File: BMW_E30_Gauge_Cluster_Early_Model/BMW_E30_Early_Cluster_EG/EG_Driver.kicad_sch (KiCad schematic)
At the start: 24 parts, among them Q2 BC337, U1 4049, U2 4584, U3 SAJ300R, U4 LM2903, U6 PIC1655A, Y1 160 kHz

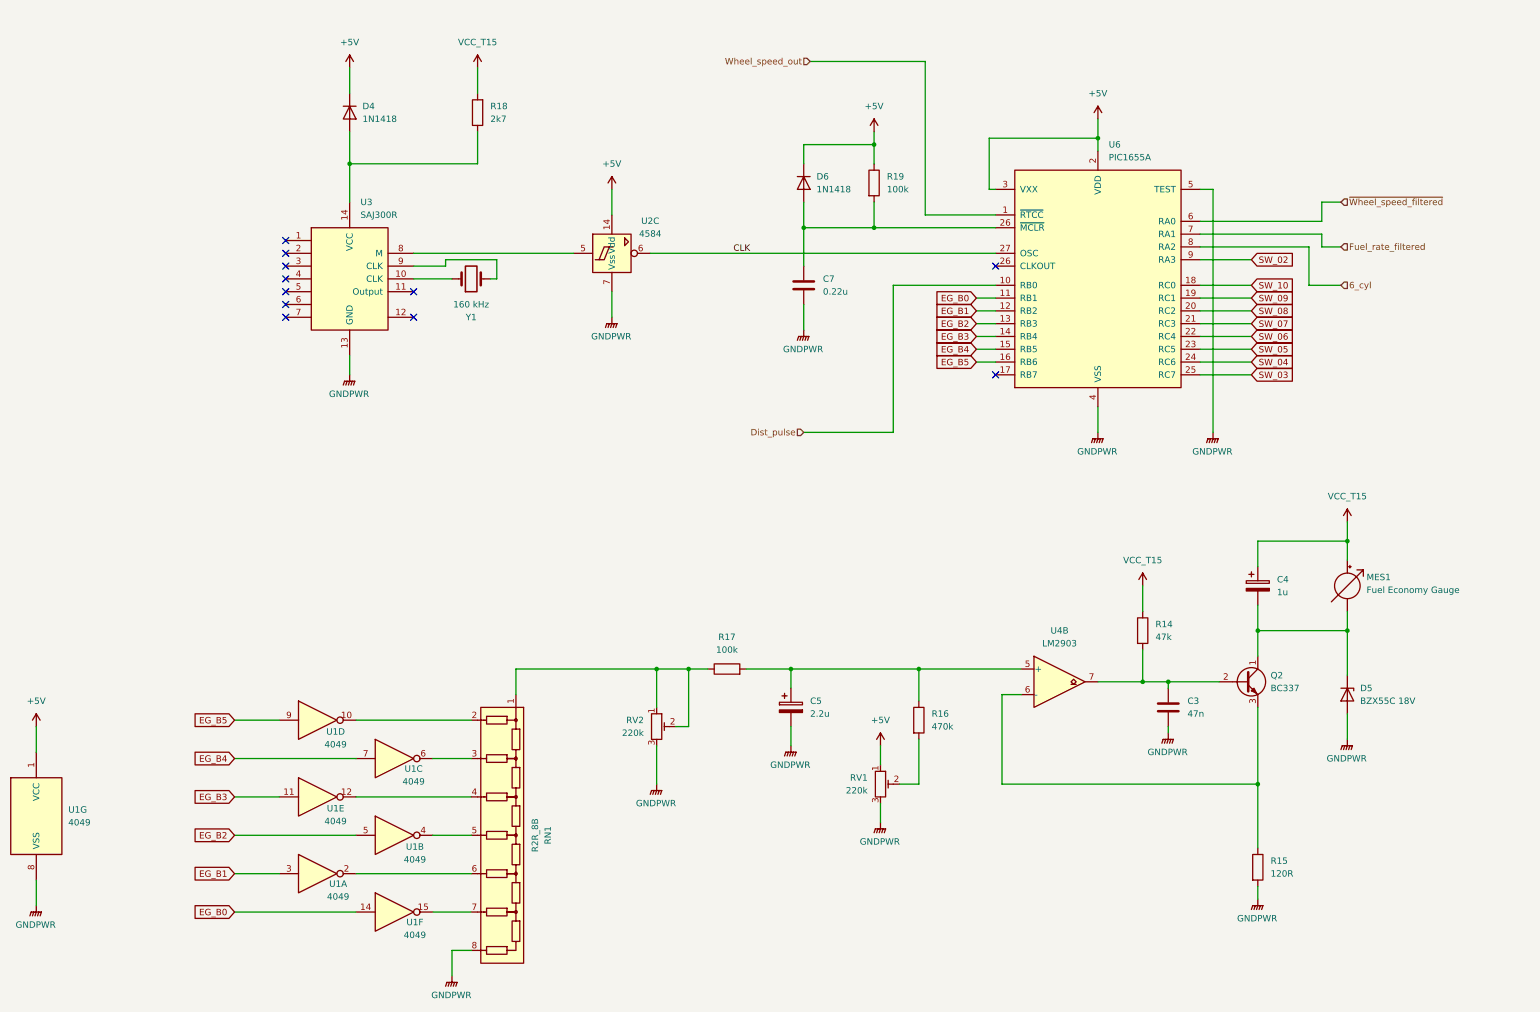
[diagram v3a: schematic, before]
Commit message: Layout Updates
Added footprints for coding plug, econometer gauge, and D5.

Also fixed pin number 28 on U6.
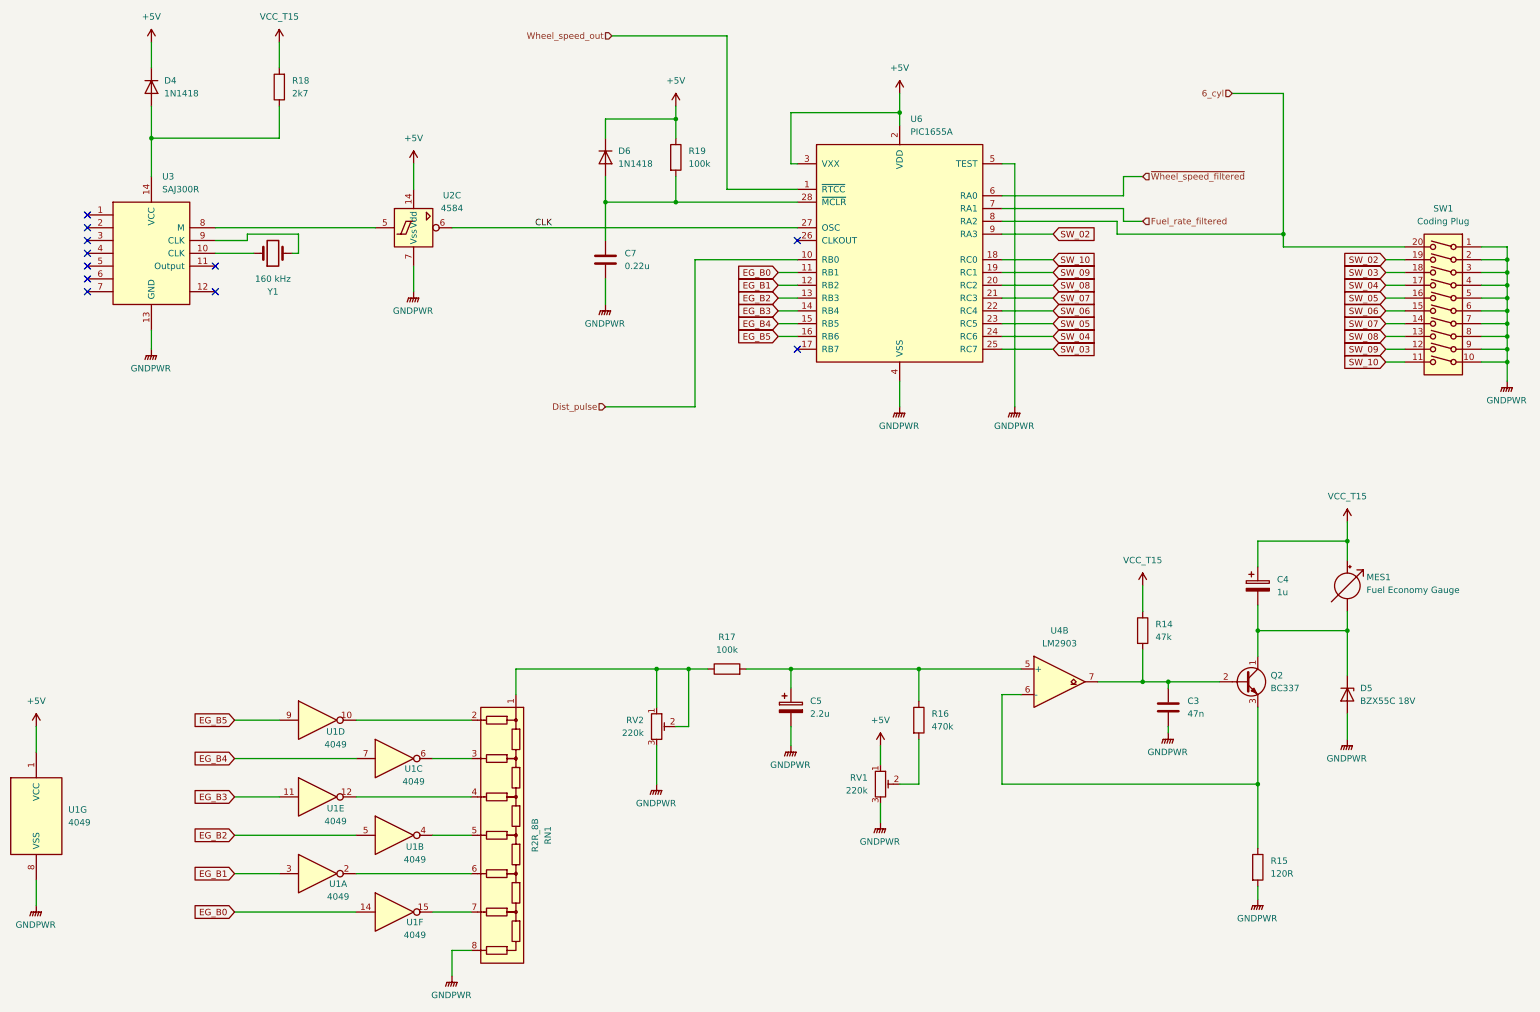
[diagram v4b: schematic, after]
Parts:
- added SW1: Coding Plug, BMW_Cluster_Connectors:Coding_Plug, symbol Switch:SW_DIP_x10
- D5: footprint (none) -> Diode_THT:D_DO-34_SOD68_P10.16mm_Horizontal
- MES1: footprint (none) -> BMW_Cluster_Connectors:Connector_EG
- U6: footprint Package_DIP:DIP-28_W15.24mm_Socket_LongPads -> Package_DIP:DIP-28_W15.24mm
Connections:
- net 6_cyl: now also SW1.20
- net GNDPWR: now also SW1.1, SW1.10, SW1.2, SW1.3, SW1.4, SW1.5, SW1.6, SW1.7, SW1.8, SW1.9
- net SW_02: now also SW1.19
- net SW_03: now also SW1.18
- net SW_04: now also SW1.17
- net SW_05: now also SW1.16
- net SW_06: now also SW1.15
- net SW_07: now also SW1.14
- net SW_08: now also SW1.13
- net SW_09: now also SW1.12
- net SW_10: now also SW1.11
- net at C7.1, D6.2 (A), R19.2: now also U6.28 (~{MCLR}); no longer U6.26 (CLKOUT)
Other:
- moved on the sheet: C7, D4, D6, R18, R19, U2C, U3, U6, Y1

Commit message: Layout Updates for EG
Added footprints for J1 and J2 connectors. Also Changed footprint for RN1 to match original board. Next step is to route traces.
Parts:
- C3: footprint Capacitor_THT:C_Rect_L11.5mm_W3.6mm_P10.00mm_MKT -> Capacitor_THT:C_Rect_L13.0mm_W4.0mm_P10.00mm_FKS3_FKP3_MKS4
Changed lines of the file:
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@@
 			)
 		)
-		(property "Footprint" "Capacitor_THT:C_Rect_L11.5mm_W3.6mm_P10.00mm_MKT"
+		(property "Footprint" "Capacitor_THT:C_Rect_L13.0mm_W4.0mm_P10.00mm_FKS3_FKP3_MKS4"
 			(at 284.1752 176.53 0)
 			(effects

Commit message: Layout Updates
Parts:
- U1: footprint Package_DIP:DIP-16_W7.62mm_Socket_LongPads -> Package_DIP:DIP-16_W7.62mm_Socket
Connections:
- net GNDPWR: now also RN1.1 (Bit_out); no longer RN1.8 (R7)
- net at R17.1, RV2.1, RV2.2: now also RN1.8 (R7); no longer RN1.1 (Bit_out)
- net at U1.15: now also RN1.2 (R1); no longer RN1.7 (R6)
- net at U1.6: now also RN1.6 (R5); no longer RN1.3 (R2)
- net at U1.10: now also RN1.7 (R6); no longer RN1.2 (R1)
- net at RN1.4 (R3): now also U1.4; no longer U1.12
- net at RN1.5 (R4): now also U1.12; no longer U1.4
- net at U1.2: now also RN1.3 (R2); no longer RN1.6 (R5)
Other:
- moved on the sheet: RN1
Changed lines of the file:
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@@
 	)
 	(junction
-		(at 181.61 165.1)
-		(diameter 0)
-		(color 0 0 0 0)
-	)
-	(junction
 		(at 350.52 96.52)
 		(diameter 0)
@@
 	)
 	(junction
+		(at 181.61 165.1)
+		(diameter 0)
+		(color 0 0 0 0)
+	)
+	(junction
 		(at 350.52 83.82)
 		(diameter 0)
@@
 	(wire
 		(pts
-			(xy 121.92 190.5) (xy 144.78 190.5)
+			(xy 137.16 167.64) (xy 137.16 161.29)
 		)
 		(stroke
@@
 	(wire
 		(pts
-			(xy 97.79 213.36) (xy 121.92 213.36)
+			(xy 137.16 161.29) (xy 158.75 161.29)
 		)
 		(stroke
@@
 	(wire
 		(pts
-			(xy 153.67 165.1) (xy 153.67 170.18)
+			(xy 97.79 213.36) (xy 121.92 213.36)
 		)
 		(stroke
@@
 	(wire
 		(pts
-			(xy 137.16 213.36) (xy 144.78 213.36)
-		)
-		(stroke
-			(width 0)
-			(type default)
-		)
-	)
-	(wire
-		(pts
 			(xy 250.19 99.06) (xy 260.35 99.06)
 		)
@@
 	(wire
 		(pts
+			(xy 121.92 175.26) (xy 139.7 175.26)
+		)
+		(stroke
+			(width 0)
+			(type default)
+		)
+	)
+	(wire
+		(pts
 			(xy 97.79 198.12) (xy 121.92 198.12)
 		)
@@
 	(wire
 		(pts
+			(xy 121.92 190.5) (xy 139.7 190.5)
+		)
+		(stroke
+			(width 0)
+			(type default)
+		)
+	)
+	(wire
+		(pts
 			(xy 345.44 101.6) (xy 350.52 101.6)
 		)
@@
 	(wire
 		(pts
-			(xy 318.77 157.48) (xy 300.99 157.48)
+			(xy 137.16 198.12) (xy 139.7 198.12)
 		)
 		(stroke
@@
 	(wire
 		(pts
-			(xy 58.42 207.01) (xy 58.42 212.09)
+			(xy 318.77 157.48) (xy 300.99 157.48)
 		)
 		(stroke
@@
 	(wire
 		(pts
-			(xy 81.28 59.69) (xy 81.28 67.31)
+			(xy 58.42 207.01) (xy 58.42 212.09)
 		)
 		(stroke
@@
 	(wire
 		(pts
-			(xy 208.28 168.91) (xy 208.28 165.1)
+			(xy 81.28 59.69) (xy 81.28 67.31)
 		)
 		(stroke
@@
 	(wire
 		(pts
-			(xy 121.92 205.74) (xy 144.78 205.74)
+			(xy 208.28 168.91) (xy 208.28 165.1)
 		)
 		(stroke
@@
 	(wire
 		(pts
-			(xy 153.67 165.1) (xy 181.61 165.1)
+			(xy 139.7 167.64) (xy 137.16 167.64)
 		)
 		(stroke
@@
 	(wire
 		(pts
-			(xy 181.61 165.1) (xy 187.96 165.1)
+			(xy 158.75 161.29) (xy 158.75 165.1)
 		)
 		(stroke
@@
 	(wire
 		(pts
-			(xy 205.74 88.9) (xy 209.55 88.9)
+			(xy 181.61 165.1) (xy 187.96 165.1)
 		)
 		(stroke
@@
 	(wire
 		(pts
-			(xy 300.99 152.4) (xy 300.99 157.48)
+			(xy 205.74 88.9) (xy 209.55 88.9)
 		)
 		(stroke
@@
 	(wire
 		(pts
-			(xy 137.16 182.88) (xy 144.78 182.88)
+			(xy 300.99 152.4) (xy 300.99 157.48)
 		)
 		(stroke
@@
 	(wire
 		(pts
-			(xy 140.97 226.06) (xy 140.97 220.98)
+			(xy 148.59 223.52) (xy 148.59 218.44)
+		)
+		(stroke
+			(width 0)
+			(type default)
+		)
+	)
+	(wire
+		(pts
+			(xy 158.75 165.1) (xy 181.61 165.1)
+		)
+		(stroke
+			(width 0)
+			(type default)
+		)
+	)
+	(wire
+		(pts
+			(xy 121.92 205.74) (xy 139.7 205.74)
 		)
 		(stroke
@@
 	(wire
 		(pts
+			(xy 137.16 182.88) (xy 139.7 182.88)
+		)
+		(stroke
+			(width 0)
+			(type default)
+		)
+	)
+	(wire
+		(pts
 			(xy 110.49 82.55) (xy 110.49 78.74)
 		)
@@
 	(wire
 		(pts
-			(xy 137.16 198.12) (xy 144.78 198.12)
-		)
-		(stroke
-			(width 0)
-			(type default)
-		)
-	)
-	(wire
-		(pts
 			(xy 345.44 99.06) (xy 350.52 99.06)
 		)
@@
 	(wire
 		(pts
+			(xy 137.16 213.36) (xy 139.7 213.36)
+		)
+		(stroke
+			(width 0)
+			(type default)
+		)
+	)
+	(wire
+		(pts
 			(xy 250.19 170.18) (xy 250.19 187.96)
 		)
@@
 	(wire
 		(pts
-			(xy 121.92 175.26) (xy 144.78 175.26)
-		)
-		(stroke
-			(width 0)
-			(type default)
-		)
-	)
-	(wire
-		(pts
 			(xy 250.19 101.6) (xy 260.35 101.6)
 		)
@@
 	(wire
 		(pts
-			(xy 140.97 220.98) (xy 144.78 220.98)
-		)
-		(stroke
-			(width 0)
-			(type default)
-		)
-	)
-	(wire
-		(pts
 			(xy 318.77 153.67) (xy 318.77 157.48)
 		)
@@
 			)
 		)
-		(property "Footprint" "Package_DIP:DIP-16_W7.62mm_Socket_LongPads"
+		(property "Footprint" "Package_DIP:DIP-16_W7.62mm_Socket"
 			(at 129.54 213.36 0)
 			(effects
@@
 			)
 		)
-		(property "Footprint" "Package_DIP:DIP-16_W7.62mm_Socket_LongPads"
+		(property "Footprint" "Package_DIP:DIP-16_W7.62mm_Socket"
 			(at 129.54 182.88 0)
 			(effects
@@
 			)
 		)
-		(property "Footprint" "Package_DIP:DIP-16_W7.62mm_Socket_LongPads"
+		(property "Footprint" "Package_DIP:DIP-16_W7.62mm_Socket"
 			(at 114.3 175.26 0)
 			(effects
@@
 	(symbol
 		(lib_id "BMW_ICs:R2R_8B")
-		(at 149.86 198.12 270)
+		(at 144.78 190.5 270)
+		(mirror x)
 		(unit 1)
 		(exclude_from_sim no)
@@
 		(dnp no)
 		(property "Reference" "RN1"
-			(at 160.02 198.12 0)
+			(at 154.94 190.5 0)
 			(effects
 				(font
@@
 		)
 		(property "Value" "R2R_8B"
-			(at 157.48 198.12 0)
+			(at 152.4 190.5 0)
 			(effects
 				(font
@@
 		)
 		(property "Footprint" "Resistor_THT:R_Array_SIP8"
-			(at 158.496 198.12 0)
+			(at 153.416 190.5 0)
 			(effects
 				(font
@@
 		)
 		(property "Datasheet" ""
-			(at 149.86 198.12 0)
+			(at 144.78 190.5 0)
 			(effects
 				(font
@@
 		)
 		(property "Description" "R=100k"
-			(at 149.86 198.12 0)
+			(at 144.78 190.5 0)
 			(effects
 				(font
@@
 			)
 		)
-		(property "Footprint" "Package_DIP:DIP-16_W7.62mm_Socket_LongPads"
+		(property "Footprint" "Package_DIP:DIP-16_W7.62mm_Socket"
 			(at 114.3 190.5 0)
 			(effects
@@
 			)
 		)
-		(property "Footprint" "Package_DIP:DIP-16_W7.62mm_Socket_LongPads"
+		(property "Footprint" "Package_DIP:DIP-16_W7.62mm_Socket"
 			(at 129.54 198.12 0)
 			(effects
@@
 	(symbol
 		(lib_id "power:GNDPWR")
-		(at 140.97 226.06 0)
+		(at 148.59 223.52 0)
 		(unit 1)
 		(exclude_from_sim no)
@@
 		(fields_autoplaced yes)
 		(property "Reference" "#PWR044"
-			(at 140.97 231.14 0)
+			(at 148.59 228.6 0)
 			(effects
 				(font
@@
 		)
 		(property "Value" "GNDPWR"
-			(at 140.843 229.87 0)
+			(at 148.463 227.33 0)
 			(effects
 				(font
@@
 		)
 		(property "Footprint" ""
-			(at 140.97 227.33 0)
+			(at 148.59 224.79 0)
 			(effects
 				(font
@@
 		)
 		(property "Datasheet" ""
-			(at 140.97 227.33 0)
+			(at 148.59 224.79 0)
 			(effects
 				(font
@@
 		)
 		(property "Description" "Power symbol creates a global label with name \"GNDPWR\" , global ground"
-			(at 140.97 226.06 0)
+			(at 148.59 223.52 0)
 			(effects
 				(font
@@
 			)
 		)
-		(property "Footprint" "Package_DIP:DIP-16_W7.62mm_Socket_LongPads"
+		(property "Footprint" "Package_DIP:DIP-16_W7.62mm_Socket"
 			(at 58.42 194.31 0)
 			(effects
@@
 			)
 		)
-		(property "Footprint" "Package_DIP:DIP-16_W7.62mm_Socket_LongPads"
+		(property "Footprint" "Package_DIP:DIP-16_W7.62mm_Socket"
 			(at 114.3 205.74 0)
 			(effects

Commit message: Update Schematic PDFs
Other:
- company: Reagan Ansel -> Reans
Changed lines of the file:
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@@
 	(title_block
 		(title "BMW E30 Gauge Cluster Fuel Economy Gauge")
-		(company "Reagan Ansel")
-		(comment 1 "NOTE: All resistors are 5% tolorance unless otherwise noted")
+		(date "2026-06-03")
+		(company "Reans")
+		(comment 1 "Reagan Ansel")
+		(comment 2 "NOTE: All resistors are 5% tolorance unless otherwise noted")
 	)
 	(junction
@@
 		)
 		(instances
-			(project ""
+			(project "BMW_E30_Early_Cluster_EG"
 				(path "/b216cb44-2546-4a52-a541-225697d17737/523a037d-2c6e-49de-a758-40f01dbf4536"
 					(reference "SW1")
